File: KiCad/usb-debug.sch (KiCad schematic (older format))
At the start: 76 parts, among them IC1 TPS7A0518PDBVT, IC16 AP22652W6-7, IC7 HD3SS3220, J11 632723300011, J5 632723300011, J9 632723300011, Q1 PMV32UP, T6 BSS138APW, T7 BSS138APW, U10 TPD4E05U06QDQARQ1, U11 TPD4E05U06QDQARQ1, U12 TPD4E05U06QDQARQ1, U13 TPD4E05U06QDQARQ1, U8 TPD4E05U06QDQARQ1, U9 TPD4E05U06QDQARQ1

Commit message: Loclib
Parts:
- IC1: footprint antmicro-footprints:SOT-23-5 -> jetson-nano-baseboard-footprints:SOT-23-5; symbol antmicroPMICVoltageRegulatorsLinear:TPS7A0518PDBVT -> jetson-nano-baseboard:TPS7A0518PDBVT
- U10, U11, U12, U13, U8, U9: footprint antmicro-footprints:TPD4E05U06QDQARQ1 -> jetson-nano-baseboard-footprints:TPD4E05U06QDQARQ1; symbol antmicroTVSDiodes:TPD4E05U06QDQARQ1 -> jetson-nano-baseboard:TPD4E05U06QDQARQ1
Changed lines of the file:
@@
 $EndComp
 $Comp
-L antmicroTVSDiodes:TPD4E05U06QDQARQ1 U8
+L jetson-nano-baseboard:TPD4E05U06QDQARQ1 U8
 U 1 1 61FB5553
 P 6825 6650
 F 0 "U8" V 7198 6650 50  0000 C CNN
 F 1 "TPD4E05U06QDQARQ1" H 6875 6250 50  0001 L CNN
-F 2 "antmicro-footprints:TPD4E05U06QDQARQ1" H 6875 7100 50  0001 L CNN
+F 2 "jetson-nano-baseboard-footprints:TPD4E05U06QDQARQ1" H 6875 7100 50  0001 L CNN
 F 3 "http://www.ti.com/general/docs/lit/getliterature.tsp?genericPartNumber=TPD4E001&fileType=pdf" H 6825 7050 50  0001 L CNN
 F 4 "Texas Instruments" V 7289 6650 50  0000 C CNN "Manufacturer"
@@
 $EndComp
 $Comp
-L antmicroTVSDiodes:TPD4E05U06QDQARQ1 U10
+L jetson-nano-baseboard:TPD4E05U06QDQARQ1 U10
 U 1 1 61FBEC77
 P 10275 4475
 F 0 "U10" H 10392 5030 50  0000 C CNN
 F 1 "TPD4E05U06QDQARQ1" H 10325 4075 50  0001 L CNN
-F 2 "antmicro-footprints:TPD4E05U06QDQARQ1" H 10325 4925 50  0001 L CNN
+F 2 "jetson-nano-baseboard-footprints:TPD4E05U06QDQARQ1" H 10325 4925 50  0001 L CNN
 F 3 "http://www.ti.com/general/docs/lit/getliterature.tsp?genericPartNumber=TPD4E001&fileType=pdf" H 10275 4875 50  0001 L CNN
 F 4 "Texas Instruments" H 10392 4939 50  0000 C CNN "Manufacturer"
@@
 $EndComp
 $Comp
-L antmicroTVSDiodes:TPD4E05U06QDQARQ1 U11
+L jetson-nano-baseboard:TPD4E05U06QDQARQ1 U11
 U 1 1 61FE29FF
 P 11925 4675
 F 0 "U11" H 12042 5230 50  0000 C CNN
 F 1 "TPD4E05U06QDQARQ1" H 11975 4275 50  0001 L CNN
-F 2 "antmicro-footprints:TPD4E05U06QDQARQ1" H 11975 5125 50  0001 L CNN
+F 2 "jetson-nano-baseboard-footprints:TPD4E05U06QDQARQ1" H 11975 5125 50  0001 L CNN
 F 3 "http://www.ti.com/general/docs/lit/getliterature.tsp?genericPartNumber=TPD4E001&fileType=pdf" H 11925 5075 50  0001 L CNN
 F 4 "Texas Instruments" H 12042 5139 50  0000 C CNN "Manufacturer"
@@
 $EndComp
 $Comp
-L antmicroTVSDiodes:TPD4E05U06QDQARQ1 U13
+L jetson-nano-baseboard:TPD4E05U06QDQARQ1 U13
 U 1 1 61FF8D6D
 P 13700 4675
 F 0 "U13" H 13817 5230 50  0000 C CNN
 F 1 "TPD4E05U06QDQARQ1" H 13750 4275 50  0001 L CNN
-F 2 "antmicro-footprints:TPD4E05U06QDQARQ1" H 13750 5125 50  0001 L CNN
+F 2 "jetson-nano-baseboard-footprints:TPD4E05U06QDQARQ1" H 13750 5125 50  0001 L CNN
 F 3 "http://www.ti.com/general/docs/lit/getliterature.tsp?genericPartNumber=TPD4E001&fileType=pdf" H 13700 5075 50  0001 L CNN
 F 4 "Texas Instruments" H 13817 5139 50  0000 C CNN "Manufacturer"
@@
 	12500 7175 12200 7175
 $Comp
-L antmicroTVSDiodes:TPD4E05U06QDQARQ1 U12
+L jetson-nano-baseboard:TPD4E05U06QDQARQ1 U12
 U 1 1 62017093
 P 12700 7275
 F 0 "U12" V 13100 6950 50  0000 L CNN
 F 1 "TPD4E05U06QDQARQ1" H 12750 6875 50  0001 L CNN
-F 2 "antmicro-footprints:TPD4E05U06QDQARQ1" H 12750 7725 50  0001 L CNN
+F 2 "jetson-nano-baseboard-footprints:TPD4E05U06QDQARQ1" H 12750 7725 50  0001 L CNN
 F 3 "http://www.ti.com/general/docs/lit/getliterature.tsp?genericPartNumber=TPD4E001&fileType=pdf" H 12700 7675 50  0001 L CNN
 F 4 "Texas Instruments" V 13200 6950 50  0000 L CNN "Manufacturer"
@@
 	6725 5950 6725 6600
 $Comp
-L antmicroTVSDiodes:TPD4E05U06QDQARQ1 U9
+L jetson-nano-baseboard:TPD4E05U06QDQARQ1 U9
 U 1 1 6231E4F6
 P 7825 6650
 F 0 "U9" V 8198 6650 50  0000 C CNN
 F 1 "TPD4E05U06QDQARQ1" H 7875 6250 50  0001 L CNN
-F 2 "antmicro-footprints:TPD4E05U06QDQARQ1" H 7875 7100 50  0001 L CNN
+F 2 "jetson-nano-baseboard-footprints:TPD4E05U06QDQARQ1" H 7875 7100 50  0001 L CNN
 F 3 "http://www.ti.com/general/docs/lit/getliterature.tsp?genericPartNumber=TPD4E001&fileType=pdf" H 7825 7050 50  0001 L CNN
 F 4 "Texas Instruments" V 8289 6650 50  0000 C CNN "Manufacturer"
@@
 5V0_DBG
 $Comp
-L antmicroPMICVoltageRegulatorsLinear:TPS7A0518PDBVT IC1
+L jetson-nano-baseboard:TPS7A0518PDBVT IC1
 U 1 1 6241F94F
 P 13700 9100
 F 0 "IC1" H 13700 9581 50  0000 C CNN
 F 1 "TPS7A0518PDBVT" H 13700 9498 39  0000 C CNN
-F 2 "antmicro-footprints:SOT-23-5" H 13700 8850 50  0001 C CNN
+F 2 "jetson-nano-baseboard-footprints:SOT-23-5" H 13700 8850 50  0001 C CNN
 F 3 "" H 13700 9100 50  0001 C CNN
 F 4 "TPS7A0518PDBVT" H 13700 9415 50  0000 C CNN "MPN"

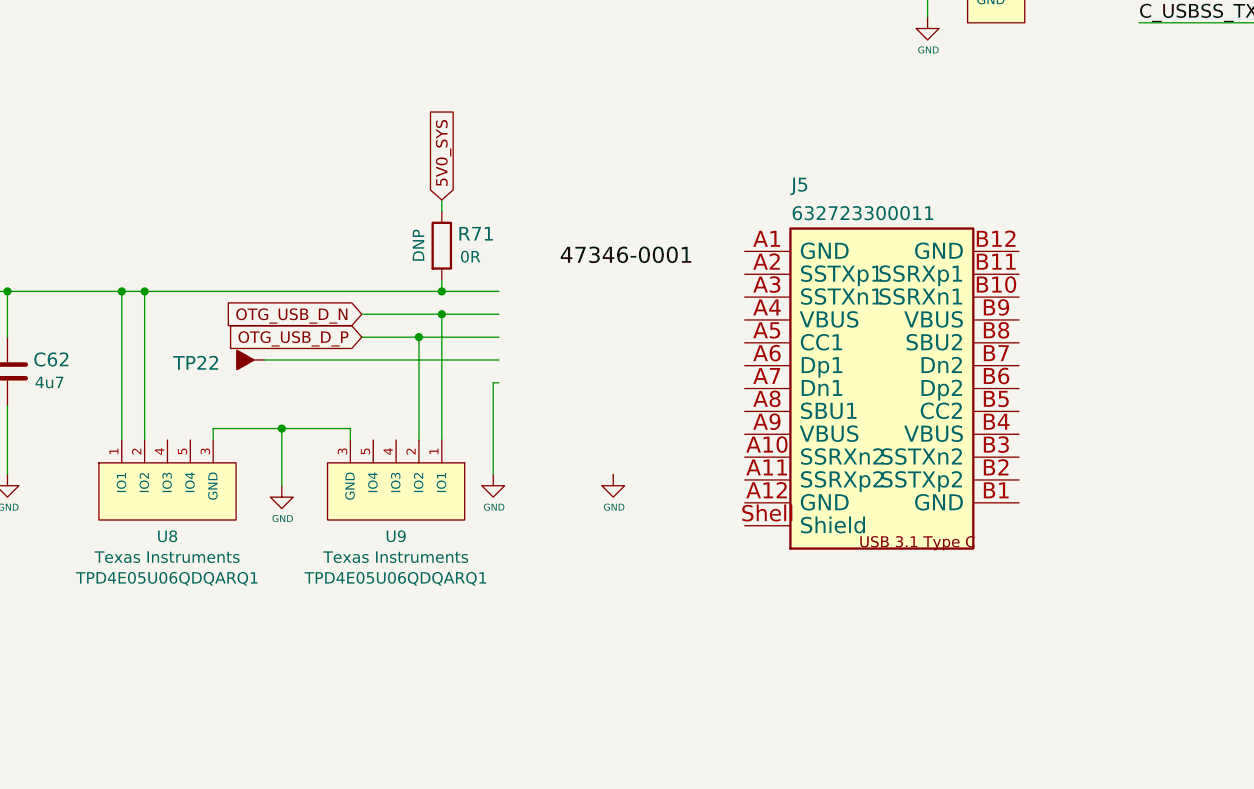
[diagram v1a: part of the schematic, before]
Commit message: Connect OTG USB and Ethernet on schematic
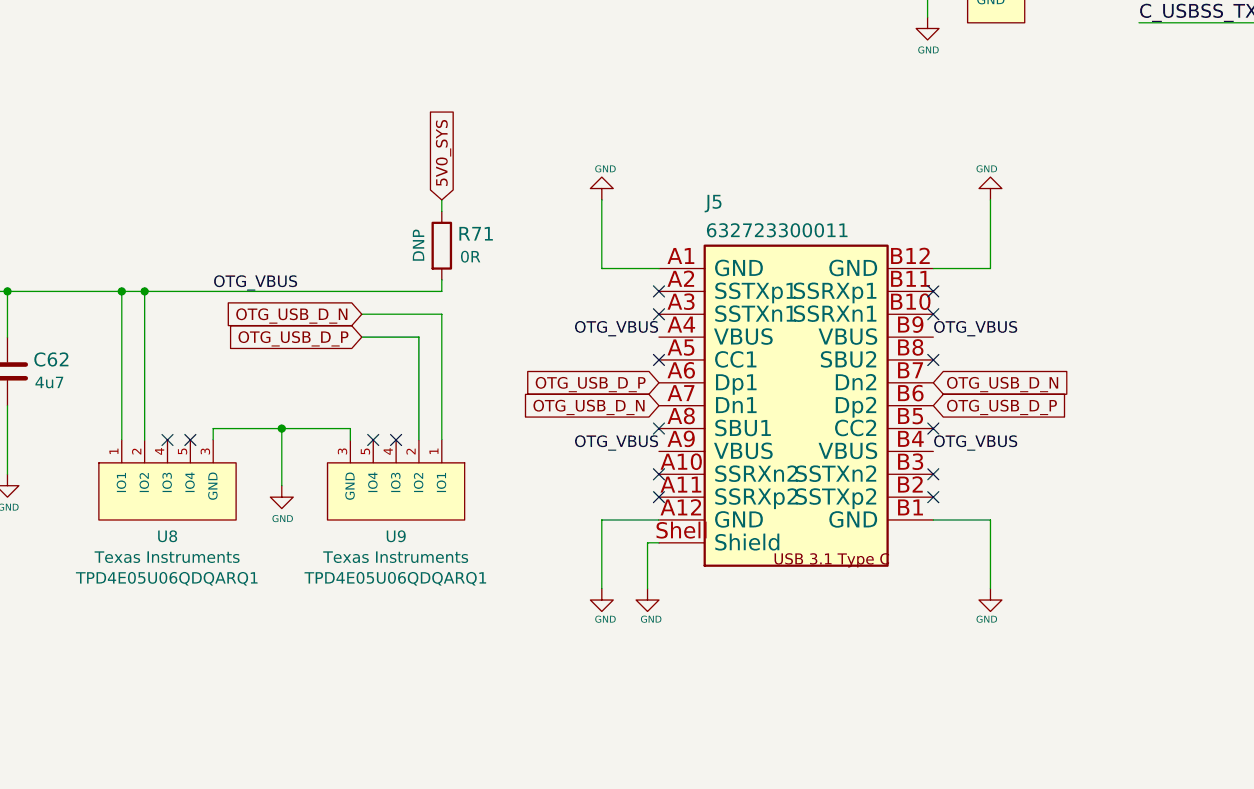
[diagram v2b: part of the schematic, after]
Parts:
- removed TP22: ~, jetson-nano-baseboard-footprints:TP-R-1.5, symbol jetson-nano-baseboard:Testpad
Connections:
- net GND: now also J5.A1 (GND), J5.A12 (GND), J5.B1 (GND), J5.B12 (GND), J5.Shell (Shield)
- net OTG_USB_D_N: now also J5.A7 (Dn1), J5.B7 (Dn2)
- net OTG_USB_D_P: now also J5.A6 (Dp1), J5.B6 (Dp2)
- net OTG_VBUS: now reaches C62.2, R71.2, R72.1, U8.1 (IO1), U8.10 (IO1), U8.2 (IO2), U8.9 (IO2)
- net OTG_VBUS: now also J5.A4 (VBUS), J5.A9 (VBUS), J5.B4 (VBUS), J5.B9 (VBUS)
- no-connect marks 29 -> 45
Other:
- moved on the sheet: J5
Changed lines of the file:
@@
 Text Label 9775 4375 0    60   ~ 0
 C_CC2
-Text Label 9125 5850 2    70   ~ 0
-47346-0001
 Text Notes 4600 5175 0    59   ~ 12
 USB-OTG
@@
 $EndComp
 $Comp
-L jetson-nano-baseboard:GND #GND_0106
-U 1 1 5E71034A
-P 8250 6750
-F 0 "#GND_0106" H 8250 6750 20  0001 C CNN
-F 1 "GND" H 8254 6605 30  0000 C CNN
-F 2 "" H 8250 6750 70  0001 C CNN
-F 3 "" H 8250 6750 70  0001 C CNN
-	1    8250 6750
-	1    0    0    -1
-$EndComp
-$Comp
 L jetson-nano-baseboard:GND #GND_0108
 U 1 1 5E710346
@@
 	1    4350 8975
 	1    0    0    -1
-$EndComp
-$Comp
-L jetson-nano-baseboard:Testpad TP22
-U 1 1 5E71031E
-P 7200 6250
-F 0 "TP22" V 7150 6600 60  0000 R TNN
-F 1 "~" H 7200 6250 50  0001 C CNN
-F 2 "jetson-nano-baseboard-footprints:TP-R-1.5" H 7200 6250 50  0001 C CNN
-F 3 "" H 7200 6250 50  0001 C CNN
-F 4 "N/A" H -31721 -13355 50  0001 C CNN "MPN"
-F 5 "N/A" H -31721 -13355 50  0001 C CNN "Manufacturer"
-	1    7200 6250
-	0    -1   -1   0
 $EndComp
 $Comp
@@
 	7675 6050 8025 6050
 Wire Wire Line
-	8275 6150 7925 6150
-Wire Wire Line
-	7250 6250 8275 6250
-Wire Wire Line
-	8275 6350 8250 6350
-Wire Wire Line
-	8250 6350 8250 6750
-Connection ~ 7925 6150
-Wire Wire Line
 	7925 6150 7675 6150
-Connection ~ 8025 6050
-Wire Wire Line
-	8025 6050 8275 6050
 Wire Wire Line
 	7325 6550 7325 6800
@@
 Wire Wire Line
 	8025 5900 8025 5950
-Connection ~ 8025 5950
-Wire Wire Line
-	8025 5950 8275 5950
 Wire Wire Line
 	8025 5600 8025 5550
@@
 	-1   0    0    -1
 $EndComp
-$Comp
-L jetson-nano-baseboard:GND #GND_0107
-U 1 1 622610D8
-P 8775 6750
-F 0 "#GND_0107" H 8775 6750 20  0001 C CNN
-F 1 "GND" H 8779 6605 30  0000 C CNN
-F 2 "" H 8775 6750 70  0001 C CNN
-F 3 "" H 8775 6750 70  0001 C CNN
-	1    8775 6750
-	1    0    0    -1
-$EndComp
 Wire Wire Line
 	6725 5950 6725 6600
@@
 F 5 "Texas Instruments" H 13700 9324 50  0000 C CNN "Manufacturer"
 	1    13700 9100
-	1    0    0    -1
-$EndComp
-$Comp
-L jetson-nano-baseboard:WE_632723300011 J5
-U 1 1 6283AAB4
-P 9550 5675
-F 0 "J5" H 9554 5830 60  0000 L BNN
-F 1 "632723300011" H 9554 5705 60  0000 L BNN
-F 2 "jetson-nano-baseboard-footprints:WE_632723300011" H 9550 5675 60  0001 C CNN
-F 3 "" H 9550 5675 60  0001 C CNN
-F 4 "Wurth Elektronik" V -1150 1082 60  0001 C CNN "Manufacturer"
-F 5 "632723300011" H -33421 -10430 50  0001 C CNN "MPN"
-	1    9550 5675
 	1    0    0    -1
 $EndComp
@@
 NoConn ~ 15650 6525
 NoConn ~ 15650 6425
+$Comp
+L jetson-nano-baseboard:GND #GND_0106
+U 1 1 61CD84AE
+P 8725 7250
+F 0 "#GND_0106" H 8725 7250 20  0001 C CNN
+F 1 "GND" H 8741 7115 30  0000 C CNN
+F 2 "" H 8725 7250 70  0001 C CNN
+F 3 "" H 8725 7250 70  0001 C CNN
+	1    8725 7250
+	1    0    0    -1
+$EndComp
+Wire Wire Line
+	8975 7050 8925 7050
+Wire Wire Line
+	8925 7050 8925 7250
+Wire Wire Line
+	8975 6950 8725 6950
+Wire Wire Line
+	8725 6950 8725 7250
+$Comp
+L jetson-nano-baseboard:GND #GND_0107
+U 1 1 61CD84CA
+P 10425 7250
+F 0 "#GND_0107" H 10425 7250 20  0001 C CNN
+F 1 "GND" H 10441 7115 30  0000 C CNN
+F 2 "" H 10425 7250 70  0001 C CNN
+F 3 "" H 10425 7250 70  0001 C CNN
+	1    10425 7250
+	-1   0    0    -1
+$EndComp
+Wire Wire Line
+	10175 6950 10425 6950
+Wire Wire Line
+	10425 6950 10425 7250
+$Comp
+L jetson-nano-baseboard:GND #GND_0126
+U 1 1 61CD84D2
+P 10425 5550
+F 0 "#GND_0126" H 10425 5550 20  0001 C CNN
+F 1 "GND" H 10441 5415 30  0000 C CNN
+F 2 "" H 10425 5550 70  0001 C CNN
+F 3 "" H 10425 5550 70  0001 C CNN
+	1    10425 5550
+	-1   0    0    1
+$EndComp
+Wire Wire Line
+	10175 5850 10425 5850
+Wire Wire Line
+	10425 5850 10425 5550
+$Comp
+L jetson-nano-baseboard:GND #GND_0139
+U 1 1 61CD84DA
+P 8725 5550
+F 0 "#GND_0139" H 8725 5550 20  0001 C CNN
+F 1 "GND" H 8741 5415 30  0000 C CNN
+F 2 "" H 8725 5550 70  0001 C CNN
+F 3 "" H 8725 5550 70  0001 C CNN
+	1    8725 5550
+	1    0    0    1
+$EndComp
+Wire Wire Line
+	8975 5850 8725 5850
+Wire Wire Line
+	8725 5850 8725 5550
+NoConn ~ 8975 5950
+NoConn ~ 8975 6050
+NoConn ~ 8975 6250
+NoConn ~ 8975 6550
+NoConn ~ 8975 6750
+NoConn ~ 8975 6850
+NoConn ~ 10175 6750
+NoConn ~ 10175 6850
+NoConn ~ 10175 6550
+NoConn ~ 10175 6250
+NoConn ~ 10175 6050
+NoConn ~ 10175 5950
+$Comp
+L jetson-nano-baseboard:WE_632723300011 J5
+U 1 1 6283AAB4
+P 9175 5750
+F 0 "J5" H 9179 5905 60  0000 L BNN
+F 1 "632723300011" H 9179 5780 60  0000 L BNN
+F 2 "jetson-nano-baseboard-footprints:WE_632723300011" H 9175 5750 60  0001 C CNN
+F 3 "" H 9175 5750 60  0001 C CNN
+F 4 "Wurth Elektronik" V -1525 1157 60  0001 C CNN "Manufacturer"
+F 5 "632723300011" H -33796 -10355 50  0001 C CNN "MPN"
+	1    9175 5750
+	1    0    0    -1
+$EndComp
+$Comp
+L jetson-nano-baseboard:GND #GND_0140
+U 1 1 61D929E4
+P 8925 7250
+F 0 "#GND_0140" H 8925 7250 20  0001 C CNN
+F 1 "GND" H 8941 7115 30  0000 C CNN
+F 2 "" H 8925 7250 70  0001 C CNN
+F 3 "" H 8925 7250 70  0001 C CNN
+	1    8925 7250
+	1    0    0    -1
+$EndComp
+Text GLabel 8975 6450 0    50   Input ~ 0
+OTG_USB_D_N
+Text GLabel 8975 6350 0    50   Input ~ 0
+OTG_USB_D_P
+Text GLabel 10175 6350 2    50   Input ~ 0
+OTG_USB_D_N
+Text GLabel 10175 6450 2    50   Input ~ 0
+OTG_USB_D_P
+Text Label 7025 5950 0    50   ~ 0
+OTG_VBUS
+Text Label 8975 6150 2    50   ~ 0
+OTG_VBUS
+Text Label 8975 6650 2    50   ~ 0
+OTG_VBUS
+Text Label 10175 6150 0    50   ~ 0
+OTG_VBUS
+Text Label 10175 6650 0    50   ~ 0
+OTG_VBUS
+NoConn ~ 7825 6600
+NoConn ~ 7725 6600
+NoConn ~ 6925 6600
+NoConn ~ 6825 6600
 $EndSCHEMATC
